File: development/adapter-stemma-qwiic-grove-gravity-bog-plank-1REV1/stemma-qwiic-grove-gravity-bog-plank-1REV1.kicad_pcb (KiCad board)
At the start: 2 copper layers, 39.5 x 51 mm, 13 parts, among them J1 SM04B-SRSS-TB (HC-1.0-4PWT), J10 ED10BGFBK, J11 Conn_01x10, J12 Conn_01x10, J2 SM04B-SRSS-TB (HC-1.0-4PWT), J3 SM04B-SRSS-TB (HC-1.0-4PWT), J4 SM04B-SRSS-TB (HC-1.0-4PWT), J6 S4B-PH-SM4-TB (HC-PH-4AWT), J7 S3B-PH-SM4-TB (HC-PH-3AWT), J8 S4B-PH-SM4-TB (HC-PH-4AWT), J9 HY-4P

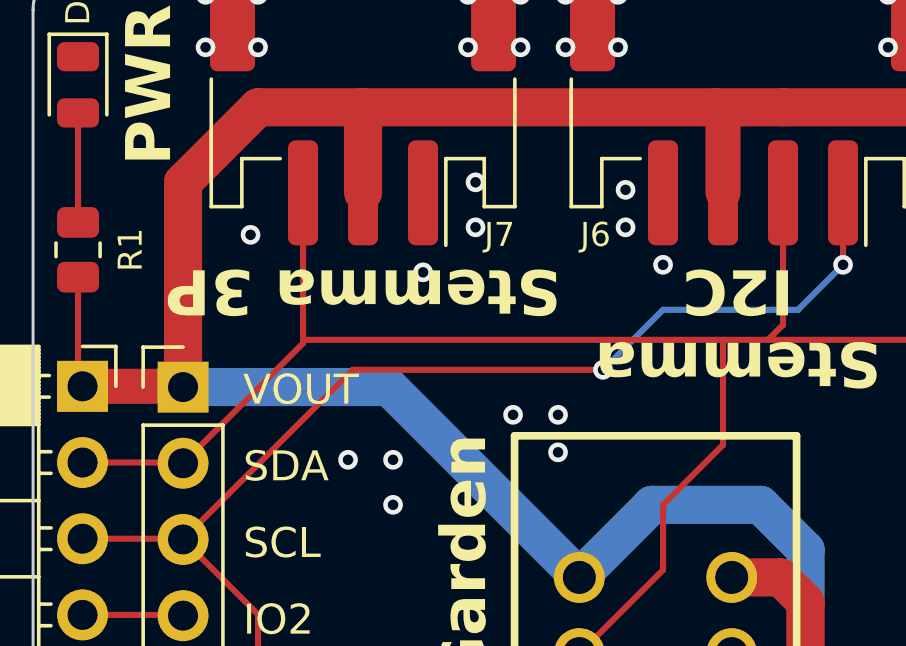
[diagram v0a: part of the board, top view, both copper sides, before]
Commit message: Change pinout on I2C quick connect
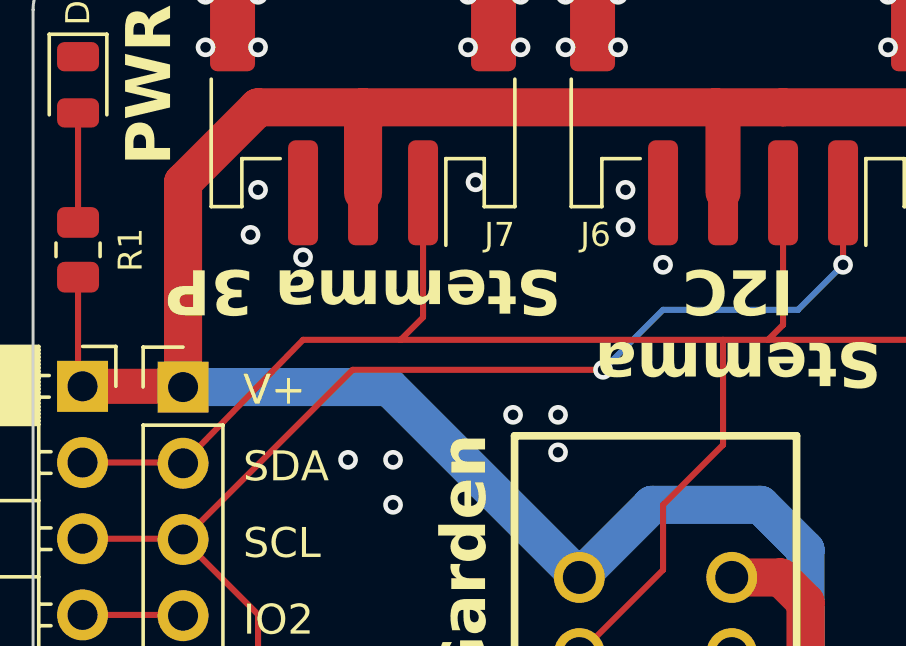
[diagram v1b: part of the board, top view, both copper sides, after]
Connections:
- J7 pad 1: GND -> SDA
- J7 pad 3: SDA -> GND
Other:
- board text added: "GND -- SCL SDA V+"
- board text added: "GND V+ SDA SCL"
- board text added: "GND V+ SIG"
- board text added: "I2C Quick Connect Plank v1 REV1 Qwiic/STEMMA (QT)/ Grove/Gravity/ Breakout Garden https://BusPirate.com"
- board text added: "SDA SCL GND V+"
- board text added: "V+"
- board text added: "V+ SDA SCL -- GND"
- board text removed: "I2C Quick Connect Plank Qwiic/STEMMA (QT)/ Grove/Gravity/ Breakout Garden https://BusPirate.com"
- board text removed: "VOUT"
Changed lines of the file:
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@@
 			(layers "F.Cu" "F.Mask" "F.Paste")
 			(roundrect_rratio 0.25)
-			(net 9 "GND")
+			(net 4 "SDA")
 			(pinfunction "Pin_1")
 			(pintype "passive")
@@
 			(layers "F.Cu" "F.Mask" "F.Paste")
 			(roundrect_rratio 0.25)
-			(net 4 "SDA")
+			(net 9 "GND")
 			(pinfunction "Pin_3")
 			(pintype "passive")
@@
 		)
 	)
-	(gr_text "VOUT"
+	(gr_text "V+"
 		(at 106.75 86.75 0)
 		(layer "F.SilkS")
@@
 		)
 	)
-	(gr_text "I2C Quick Connect Plank\nQwiic/STEMMA (QT)/\nGrove/Gravity/\nBreakout Garden\nhttps://BusPirate.com"
-		(at 111 97.5 90)
+	(gr_text "V+\nSDA\nSCL\n--\nGND"
+		(at 124.25 91.75 180)
+		(layer "B.SilkS" knockout)
+		(effects
+			(font
+				(size 1.5 1.5)
+				(thickness 0.3)
+				(bold yes)
+			)
+			(justify left bottom mirror)
+		)
+	)
+	(gr_text "GND\nV+\nSIG"
+		(at 114.25 72.5 90)
+		(layer "B.SilkS" knockout)
+		(effects
+			(font
+				(size 1.5 1.5)
+				(thickness 0.3)
+				(bold yes)
+			)
+			(justify left bottom mirror)
+		)
+	)
+	(gr_text "GND\nV+\nSDA\nSCL"
+		(at 134 107.75 180)
+		(layer "B.SilkS" knockout)
+		(effects
+			(font
+				(size 1.5 1.5)
+				(thickness 0.3)
+				(bold yes)
+			)
+			(justify left bottom mirror)
+		)
+	)
+	(gr_text "GND\n--\nSCL\nSDA\nV+"
+		(at 112 91.75 180)
+		(layer "B.SilkS" knockout)
+		(effects
+			(font
+				(size 1.5 1.5)
+				(thickness 0.3)
+				(bold yes)
+			)
+			(justify left bottom mirror)
+		)
+	)
+	(gr_text "GND\nV+\nSDA\nSCL"
+		(at 134 98 180)
+		(layer "B.SilkS" knockout)
+		(effects
+			(font
+				(size 1.5 1.5)
+				(thickness 0.3)
+				(bold yes)
+			)
+			(justify left bottom mirror)
+		)
+	)
+	(gr_text "GND\nV+\nSDA\nSCL"
+		(at 128.25 72.5 90)
+		(layer "B.SilkS" knockout)
+		(effects
+			(font
+				(size 1.5 1.5)
+				(thickness 0.3)
+				(bold yes)
+			)
+			(justify left bottom mirror)
+		)
+	)
+	(gr_text "GND\nV+\nSDA\nSCL"
+		(at 134 88.25 180)
+		(layer "B.SilkS" knockout)
+		(effects
+			(font
+				(size 1.5 1.5)
+				(thickness 0.3)
+				(bold yes)
+			)
+			(justify left bottom mirror)
+		)
+	)
+	(gr_text "I2C Quick Connect Plank v1 REV1\nQwiic/STEMMA (QT)/\nGrove/Gravity/\nBreakout Garden\nhttps://BusPirate.com"
+		(at 119.25 111.5 180)
 		(layer "B.SilkS")
 		(effects
@@
 		)
 	)
+	(gr_text "GND\nV+\nSDA\nSCL"
+		(at 127.75 117.75 90)
+		(layer "B.SilkS" knockout)
+		(effects
+			(font
+				(size 1.5 1.5)
+				(thickness 0.3)
+				(bold yes)
+			)
+			(justify left bottom mirror)
+		)
+	)
+	(gr_text "GND\nV+\nSDA\nSCL"
+		(at 134 78.5 180)
+		(layer "B.SilkS" knockout)
+		(effects
+			(font
+				(size 1.5 1.5)
+				(thickness 0.3)
+				(bold yes)
+			)
+			(justify left bottom mirror)
+		)
+	)
+	(gr_text "SDA\nSCL\nGND\nV+"
+		(at 111.5 117.75 90)
+		(layer "B.SilkS" knockout)
+		(effects
+			(font
+				(size 1.5 1.5)
+				(thickness 0.3)
+				(bold yes)
+			)
+			(justify left bottom mirror)
+		)
+	)
 	(dimension
 		(type aligned)
@@
 	)
 	(segment
-		(start 108.75 84.615)
-		(end 108.75 84.5)
-		(width 0.2032)
-		(layer "F.Cu")
-		(net 4)
-	)
-	(segment
 		(start 129.75 92)
 		(end 129.75 84.5)
@@
 	)
 	(segment
-		(start 108.75 84.5)
-		(end 108.75 79.6)
-		(width 0.2032)
-		(layer "F.Cu")
-		(net 4)
-	)
-	(segment
 		(start 124 110.25)
 		(end 124 113.1)
@@
 	)
 	(segment
+		(start 112.75 79.6)
+		(end 112.75 83.75)
+		(width 0.2032)
+		(layer "F.Cu")
+		(net 4)
+	)
+	(segment
 		(start 120.75 90)
 		(end 120.75 92.17)
@@
 	)
 	(segment
+		(start 108.75 84.5)
+		(end 112 84.5)
+		(width 0.2032)
+		(layer "F.Cu")
+		(net 4)
+	)
+	(segment
 		(start 132.25 82)
 		(end 134 82)
@@
 	)
 	(segment
+		(start 112.75 83.75)
+		(end 112 84.5)
+		(width 0.2032)
+		(layer "F.Cu")
+		(net 4)
+	)
+	(segment
 		(start 129.75 102)
 		(end 129.75 110.25)
@@
 	)
 	(segment
-		(start 108.75 84.5)
-		(end 122.75 84.5)
+		(start 122.75 88)
+		(end 120.75 90)
 		(width 0.2032)
 		(layer "F.Cu")
@@
 	)
 	(segment
-		(start 122.75 88)
-		(end 120.75 90)
+		(start 104.75 88.615)
+		(end 108.75 84.5)
 		(width 0.2032)
 		(layer "F.Cu")
@@
 	)
 	(segment
-		(start 134 102)
-		(end 129.75 102)
+		(start 112 84.5)
+		(end 122.75 84.5)
 		(width 0.2032)
 		(layer "F.Cu")
@@
 	)
 	(segment
-		(start 104.75 88.615)
-		(end 108.75 84.615)
+		(start 134 102)
+		(end 129.75 102)
 		(width 0.2032)
 		(layer "F.Cu")
@@
 	)
 	(via
-		(at 114.5 80.75)
+		(at 108.75 81.75)
 		(size 0.6548)
 		(drill 0.35)
@@
 	)
 	(via
-		(at 112.75 82.25)
+		(at 107.25 79.5)
 		(size 0.6548)
 		(drill 0.35)

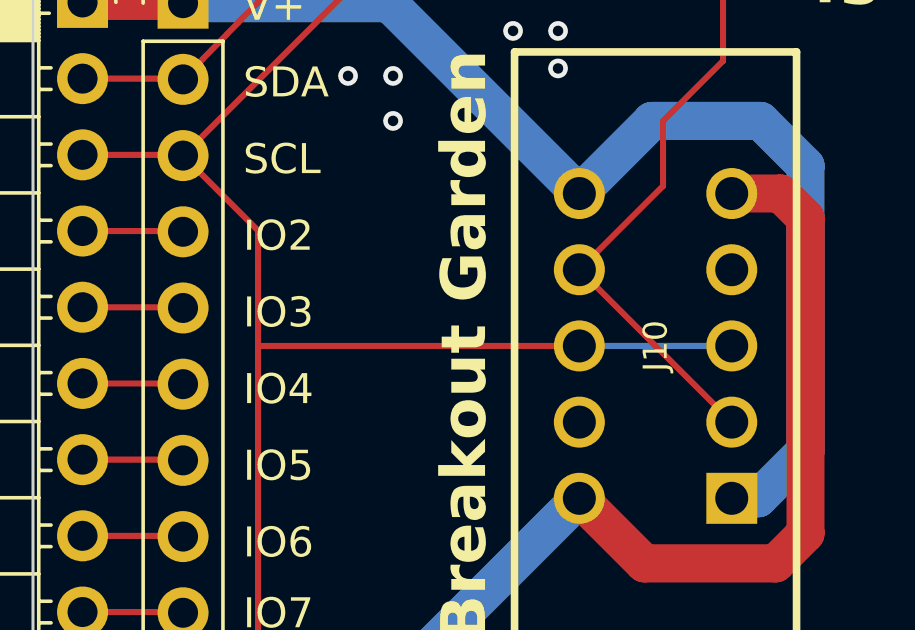
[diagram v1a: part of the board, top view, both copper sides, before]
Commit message: 7R2 with vout protection
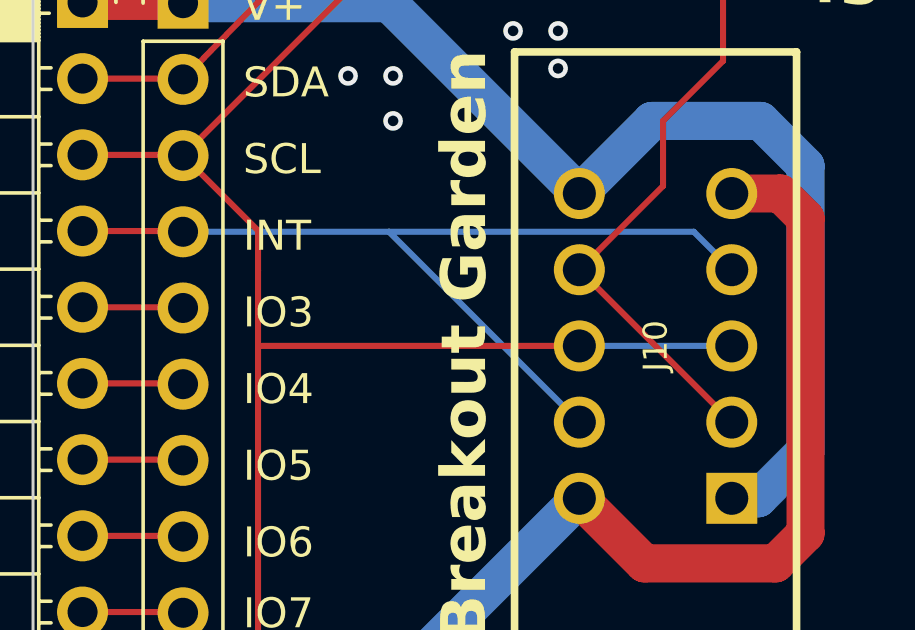
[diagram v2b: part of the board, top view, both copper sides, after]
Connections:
- J10 pad 4: unconnected-(J10-Pin_4-Pad4) -> INT
- J10 pad 7: unconnected-(J10-Pin_7-Pad7) -> INT
- J11 pad 4: IO2 -> INT
- J12 pad 4: IO2 -> INT
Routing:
- net INT: track 0.00 -> 31.1 mm
- net IO2: track 3.36 -> 0.00 mm
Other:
- board text added: "GND INT SCL SDA V+"
- board text added: "INT"
- board text added: "V+ SDA SCL INT GND"
- board text removed: "GND -- SCL SDA V+"
- board text removed: "IO2"
- board text removed: "V+ SDA SCL -- GND"
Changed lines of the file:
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@@
 	(net 0 "")
 	(net 1 "IO4")
-	(net 2 "IO2")
+	(net 2 "INT")
 	(net 3 "IO5")
 	(net 4 "SDA")
@@
 	(net 10 "VOUT")
 	(net 11 "Net-(D1-A)")
-	(net 12 "unconnected-(J10-Pin_7-Pad7)")
-	(net 13 "unconnected-(J10-Pin_4-Pad4)")
 	(footprint "footprints:CONN-SMD_HY2.0-4P"
 		(layer "F.Cu")
@@
 			(layers "*.Cu" "*.Mask")
 			(remove_unused_layers no)
-			(net 2 "IO2")
+			(net 2 "INT")
 			(pinfunction "Pin_4")
 			(pintype "passive")
@@
 			(layers "*.Cu" "*.Mask")
 			(remove_unused_layers no)
-			(net 2 "IO2")
+			(net 2 "INT")
 			(pinfunction "Pin_4")
 			(pintype "passive")
@@
 			(layers "*.Cu" "*.Paste" "*.Mask")
 			(remove_unused_layers no)
-			(net 13 "unconnected-(J10-Pin_4-Pad4)")
+			(net 2 "INT")
 			(pinfunction "Pin_4")
 			(pintype "passive")
@@
 			(layers "*.Cu" "*.Paste" "*.Mask")
 			(remove_unused_layers no)
-			(net 12 "unconnected-(J10-Pin_7-Pad7)")
+			(net 2 "INT")
 			(pinfunction "Pin_7")
 			(pintype "passive")
@@
 		)
 	)
-	(gr_text "IO2"
+	(gr_text "INT"
 		(at 106.75 94.416665 0)
 		(layer "F.SilkS")
@@
 		)
 	)
-	(gr_text "V+\nSDA\nSCL\n--\nGND"
+	(gr_text "V+\nSDA\nSCL\nINT\nGND"
 		(at 124.25 91.75 180)
 		(layer "B.SilkS" knockout)
@@
 		)
 	)
-	(gr_text "GND\n--\nSCL\nSDA\nV+"
+	(gr_text "GND\nINT\nSCL\nSDA\nV+"
 		(at 112 91.75 180)
 		(layer "B.SilkS" knockout)
@@
 		(net 2)
 	)
+	(segment
+		(start 121.775 93.695)
+		(end 123.04 94.96)
+		(width 0.2032)
+		(layer "B.Cu")
+		(net 2)
+	)
+	(segment
+		(start 117.96 100.04)
+		(end 111.615 93.695)
+		(width 0.2032)
+		(layer "B.Cu")
+		(net 2)
+	)
+	(segment
+		(start 111.615 93.695)
+		(end 121.775 93.695)
+		(width 0.2032)
+		(layer "B.Cu")
+		(net 2)
+	)
+	(segment
+		(start 111.615 93.695)
+		(end 104.75 93.695)
+		(width 0.2032)
+		(layer "B.Cu")
+		(net 2)
+	)
